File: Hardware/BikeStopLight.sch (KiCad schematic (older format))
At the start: 70 parts, among them J1 ST-Link, J2 PWR, J3 NRST, J4 Conn_01x01, J5 Conn_01x01, J6 Conn_01x08, Q1 NTD4909N, Q2 BSS138, U1 MCP1703A-3302_SOT23, U2 STM32L052K8Tx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

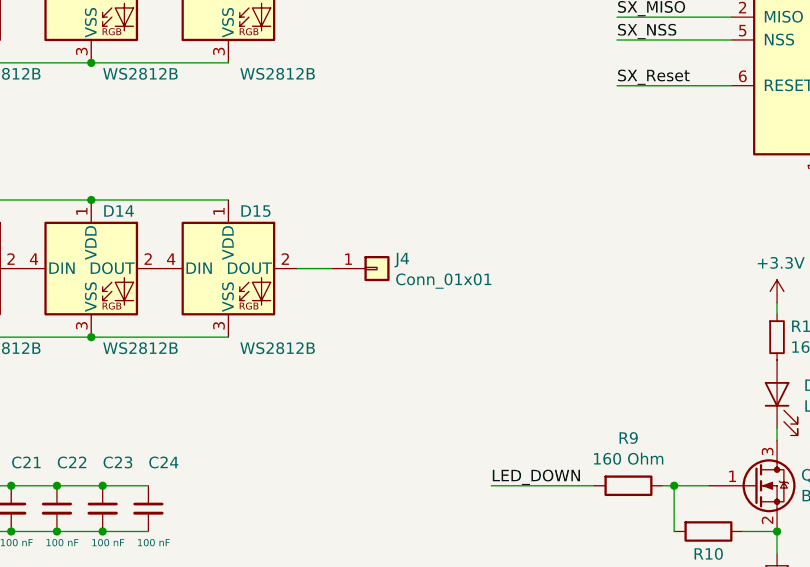
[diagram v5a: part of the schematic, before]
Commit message: Change fixing holes, silkscreen changes
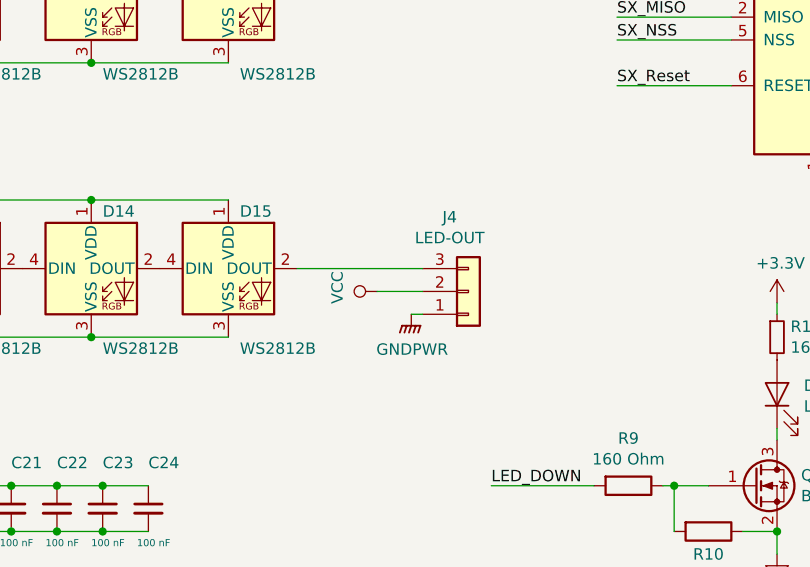
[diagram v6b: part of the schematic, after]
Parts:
- removed J4: Conn_01x01, Connector_PinHeader_2.54mm:PinHeader_1x01_P2.54mm_Vertical, symbol Connector_Generic:Conn_01x01
- added J4: LED-OUT, Connector_PinHeader_2.54mm:PinHeader_1x03_P2.54mm_Vertical, symbol Connector_Generic:Conn_01x03
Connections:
- wire segments 192 -> 194
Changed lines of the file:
@@
 	8800 5200 9350 5200
 NoConn ~ 9350 5200
-Wire Wire Line
-	4200 6250 4350 6250
-$Comp
-L Connector_Generic:Conn_01x01 J4
-U 1 1 5CE45D62
-P 4550 6250
-F 0 "J4" H 4630 6292 50  0000 L CNN
-F 1 "Conn_01x01" H 4630 6201 50  0000 L CNN
-F 2 "Connector_PinHeader_2.54mm:PinHeader_1x01_P2.54mm_Vertical" H 4550 6250 50  0001 C CNN
-F 3 "~" H 4550 6250 50  0001 C CNN
-	1    4550 6250
-	1    0    0    -1
-$EndComp
 $Comp
 L BikeStopLight-rescue:PTS645SM43SMTR92_LFS-dk_Tactile-Switches S1
@@
 	1    0    0    -1
 $EndComp
+$Comp
+L Connector_Generic:Conn_01x03 J4
+U 1 1 5D3A7BF6
+P 4950 6350
+F 0 "J4" H 4868 6025 50  0000 C CNN
+F 1 "LED-OUT" H 4868 6116 50  0000 C CNN
+F 2 "Connector_PinHeader_2.54mm:PinHeader_1x03_P2.54mm_Vertical" H 4950 6350 50  0001 C CNN
+F 3 "~" H 4950 6350 50  0001 C CNN
+	1    4950 6350
+	1    0    0    1
+$EndComp
+Wire Wire Line
+	4200 6250 4750 6250
+$Comp
+L power:GNDPWR #PWR0127
+U 1 1 5D3B7FE8
+P 4700 6450
+F 0 "#PWR0127" H 4700 6250 50  0001 C CNN
+F 1 "GNDPWR" H 4704 6296 50  0000 C CNN
+F 2 "" H 4700 6400 50  0001 C CNN
+F 3 "" H 4700 6400 50  0001 C CNN
+	1    4700 6450
+	1    0    0    -1
+$EndComp
+Wire Wire Line
+	4750 6450 4700 6450
+$Comp
+L power:VCC #PWR0128
+U 1 1 5D40B691
+P 4550 6350
+F 0 "#PWR0128" H 4550 6200 50  0001 C CNN
+F 1 "VCC" H 4567 6523 50  0000 C CNN
+F 2 "" H 4550 6350 50  0001 C CNN
+F 3 "" H 4550 6350 50  0001 C CNN
+	1    4550 6350
+	0    -1   -1   0
+$EndComp
+Wire Wire Line
+	4550 6350 4750 6350
 $EndSCHEMATC

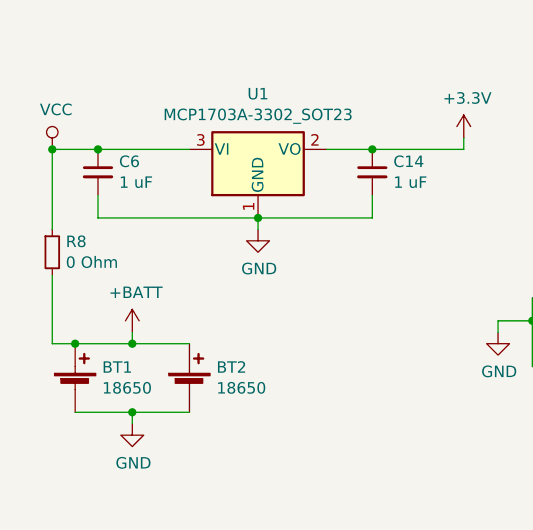
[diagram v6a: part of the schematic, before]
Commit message: Add connector for Vbat to Vcc
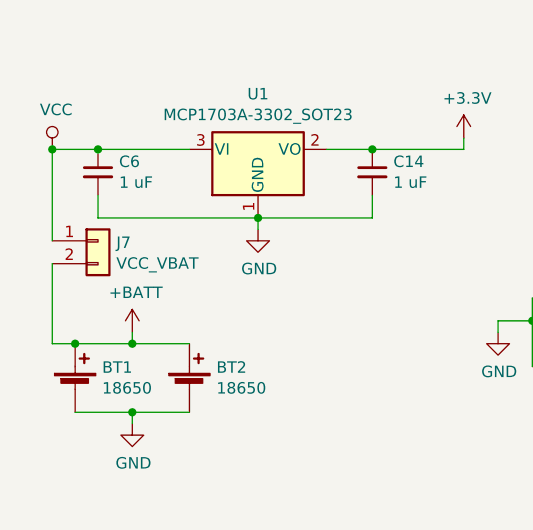
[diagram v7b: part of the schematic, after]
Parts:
- removed R8: 0 Ohm, Resistor_SMD:R_0805_2012Metric, symbol Device:R_Small
- added J7: VCC_VBAT, Connector_PinHeader_2.54mm:PinHeader_1x02_P2.54mm_Vertical, symbol Connector_Generic:Conn_01x02
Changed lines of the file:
@@
 	1    0    0    -1
 $EndComp
-$Comp
-L Device:R_Small R8
-U 1 1 5CE13172
-P 750 1550
-F 0 "R8" H 809 1596 50  0000 L CNN
-F 1 "0 Ohm" H 809 1505 50  0000 L CNN
-F 2 "Resistor_SMD:R_0805_2012Metric" H 750 1550 50  0001 C CNN
-F 3 "~" H 750 1550 50  0001 C CNN
-	1    750  1550
-	1    0    0    -1
-$EndComp
-Wire Wire Line
-	750  1450 750  1100
-Connection ~ 750  1100
-Wire Wire Line
-	750  1650 750  1950
 Wire Wire Line
 	750  1950 850  1950
@@
 Wire Wire Line
 	4550 6350 4750 6350
+$Comp
+L Connector_Generic:Conn_01x02 J7
+U 1 1 5D4A5CC8
+P 950 1500
+F 0 "J7" H 1030 1492 50  0000 L CNN
+F 1 "VCC_VBAT" H 1030 1401 50  0000 L CNN
+F 2 "Connector_PinHeader_2.54mm:PinHeader_1x02_P2.54mm_Vertical" H 950 1500 50  0001 C CNN
+F 3 "~" H 950 1500 50  0001 C CNN
+	1    950  1500
+	1    0    0    -1
+$EndComp
+Wire Wire Line
+	750  1500 750  1100
+Connection ~ 750  1100
+Wire Wire Line
+	750  1600 750  1950
 $EndSCHEMATC
